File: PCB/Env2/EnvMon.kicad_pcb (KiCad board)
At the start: 2 copper layers, 70 x 70 mm, 51 parts, among them J1 LCD, J10 Conn_01x01, J11 Conn_01x01, J12 Conn_01x01, J2 DC, J3 TEMP, J4 LCD, J5 Reset, J6 USB-C-Socket-H, J7 TC2030-USB-NL-DS, J8 T6793, J9 Conn_01x01, U1 ESP32-S3-MINI-1, U2 SCD41, U3 MD8942, U4 MCP9808_MSOP, U5 GZP6816D, U8 VEML6040

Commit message: Library update
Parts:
- J1: footprint RevK:PinSocket_1x08_P2.54mm_Vertical_SMD -> RevK:LCD2
- moved J1 0.10 mm to (73.4, 83.6)

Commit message: As ordered
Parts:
- moved J4 0.10 mm to (126.6, 83.4)
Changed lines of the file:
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@@
 	(footprint "RevK:PinHeader_1x08_P2.54mm_Vertical"
 		(layer "B.Cu")
-		(at 126.525 83.375 180)
+		(at 126.625 83.375 180)
 		(descr "Through hole straight pin header, 1x08, 2.54mm pitch, single row")
 		(tags "Through hole pin header THT 1x08 2.54mm single row")
@@
 		(layer "Edge.Cuts")
 	)
+	(gr_circle
+		(center 71 102.5)
+		(end 71.5 102.5)
+		(stroke
+			(width 0.05)
+			(type default)
+		)
+		(fill no)
+		(layer "Edge.Cuts")
+	)
+	(gr_circle
+		(center 71 83.5)
+		(end 71.5 83.5)
+		(stroke
+			(width 0.05)
+			(type default)
+		)
+		(fill no)
+		(layer "Edge.Cuts")
+	)
 	(gr_arc
 		(start 114.5 75)
@@
 	)
 	(gr_line
+		(start 71 102)
+		(end 71 84)
+		(stroke
+			(width 0.05)
+			(type solid)
+		)
+		(layer "User.2")
+	)
+	(gr_line
+		(start 71 83)
+		(end 71 77.5)
+		(stroke
+			(width 0.05)
+			(type solid)
+		)
+		(layer "User.2")
+	)
+	(gr_line
 		(start 115.5 76)
 		(end 115.5 82.5)
@@
 	(gr_line
 		(start 71 124.25)
-		(end 71 77.5)
+		(end 71 103)
 		(stroke
 			(width 0.05)
@@
 	)
 	(gr_arc
+		(start 71 102)
+		(mid 71.5 102.5)
+		(end 71 103)
+		(stroke
+			(width 0.05)
+			(type solid)
+		)
+		(layer "User.2")
+	)
+	(gr_arc
 		(start 100 79)
 		(mid 99.707107 79.707107)
@@
 		(stroke
 			(width 0.05)
+			(type solid)
+		)
+		(layer "User.2")
+	)
+	(gr_arc
+		(start 71 83)
+		(mid 71.5 83.5)
+		(end 71 84)
+		(stroke
+			(width 0.05)

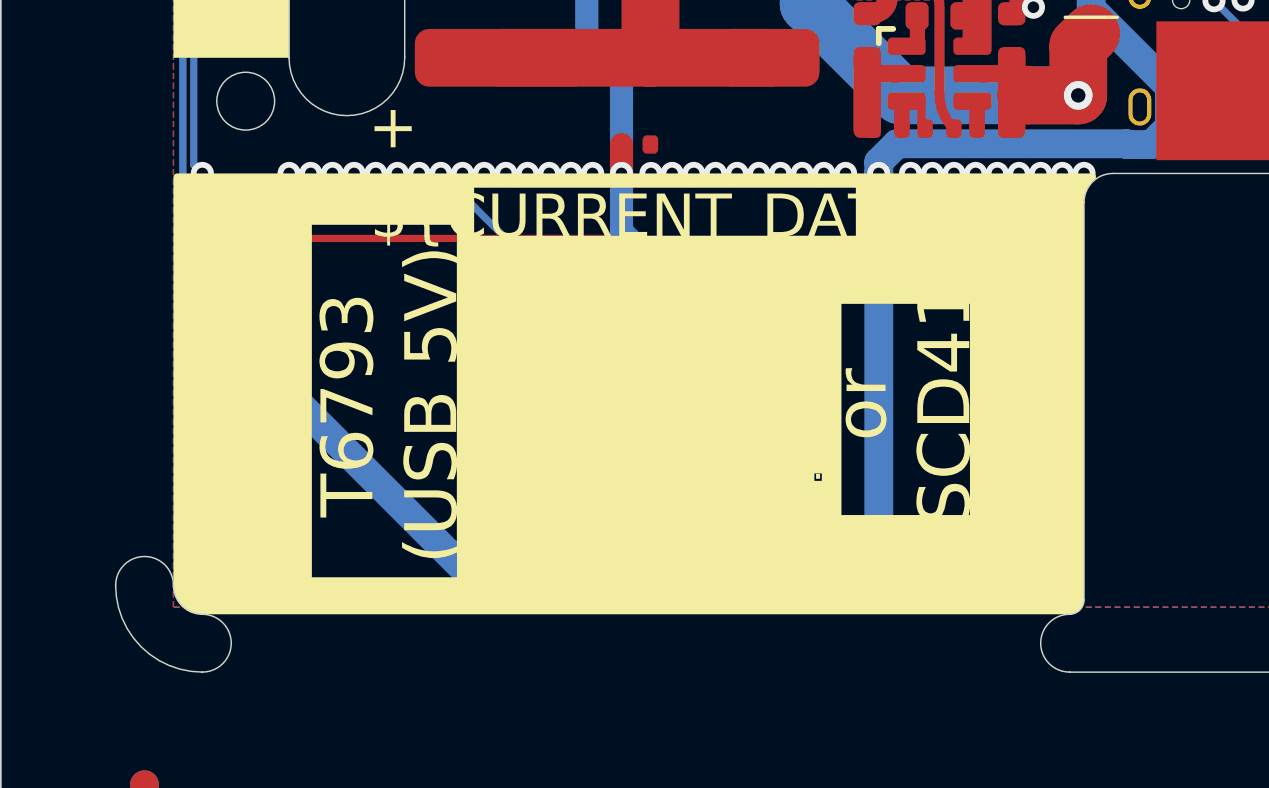
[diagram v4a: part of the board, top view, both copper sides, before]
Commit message: Moved to FaikinRemote project
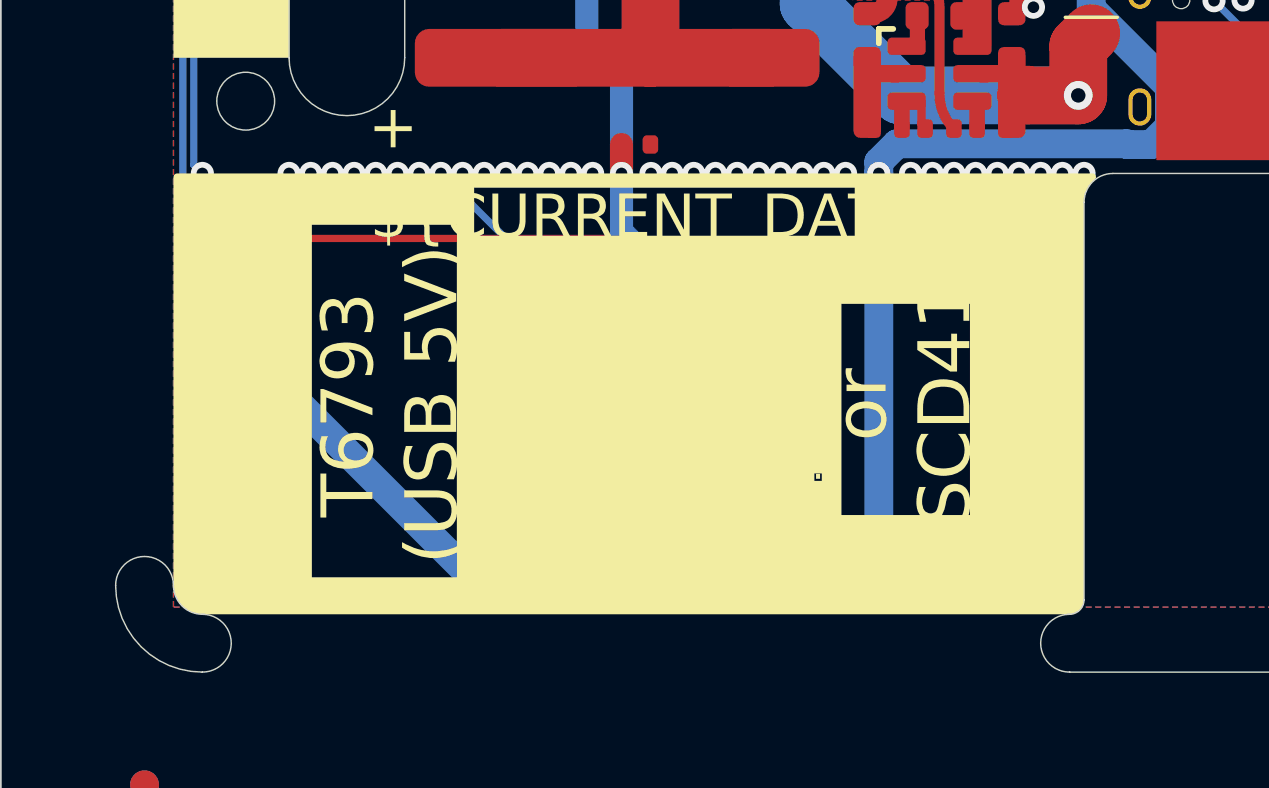
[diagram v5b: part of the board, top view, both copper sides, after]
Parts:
- D4: footprint RevK:SMD1010 -> RevK:SMD1010-Side
- U8: footprint RevK:VEML6040 -> RevK:VEML6040-Side

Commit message: New case work
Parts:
- D4: footprint RevK:SMD1010-Side -> RevK:SMD1010-Side2
- U4: footprint Package_SO:MSOP-8_3x3mm_P0.65mm -> RevK:MSOP-8_3x3mm_P0.65mm-SIde

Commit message: Library update
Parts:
- moved J1 28.0 mm to (100.0, 92.5)
